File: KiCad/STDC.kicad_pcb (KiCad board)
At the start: 4 copper layers, 38 x 48 mm, 126 parts, among them IC1 TPS22916CNYFPR, IC2 TPS22916CNYFPR, IC3 R1200N001A-TR-FE, IC4 MS5849-30BA, IC5 W25Q32JWSNIQ, J1 TC2030, J2 Conn_01x03_BATT, J3 Conn_01x34_NHD_18, Q1 AO3400A, Q2 AO3400A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

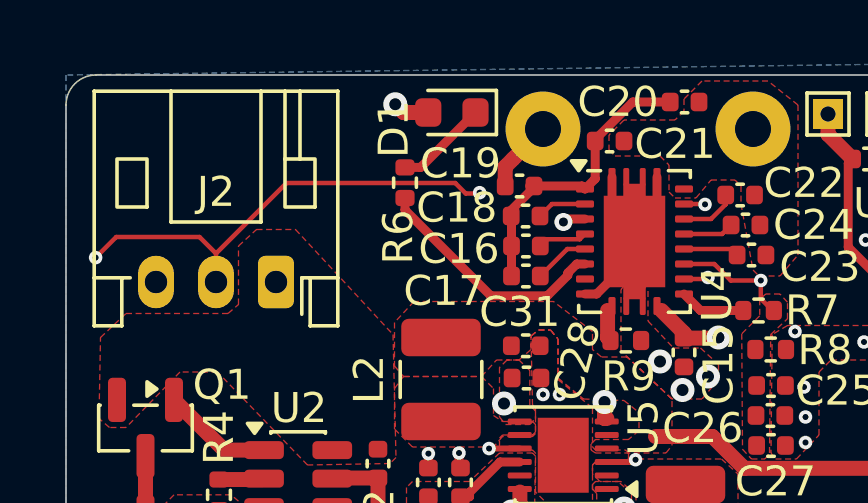
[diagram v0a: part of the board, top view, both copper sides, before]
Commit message: More space for Connector
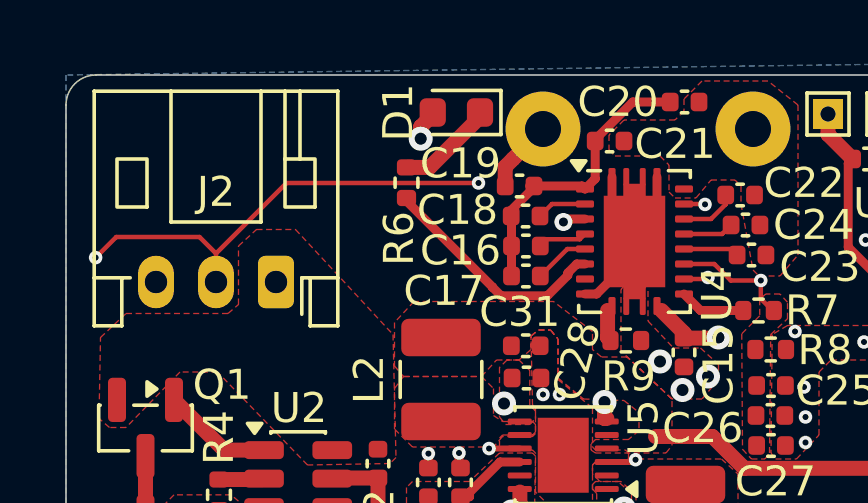
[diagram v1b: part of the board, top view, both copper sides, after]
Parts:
- moved D1 0.15 mm to (138.0, 101.8)
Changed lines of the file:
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@@
 		(tags "capacitor")
 		(property "Reference" "C16"
-			(at -2.23 0.1 0)
+			(at -2.18 0.15 0)
 			(layer "F.SilkS")
 			(effects
@@
 	(footprint "LED_SMD:LED_0603_1608Metric"
 		(layer "F.Cu")
-		(at 137.8625 101.75 180)
+		(at 138.0125 101.75 180)
 		(descr "LED SMD 0603 (1608 Metric), square (rectangular) end terminal, IPC-7351 nominal, (Body size source: http://www.tortai-tech.com/upload/download/2011102023233369053.pdf), generated with kicad-footprint-generator")
 		(tags "LED")
 		(property "Reference" "D1"
-			(at 1.9375 -0.55 90)
+			(at 1.9375 0 90)
 			(layer "F.SilkS")
 			(effects
@@
 		(tags "capacitor")
 		(property "Reference" "C18"
-			(at -2.295 -0.275 0)
+			(at -2.27 -0.2 0)
 			(layer "F.SilkS")
 			(effects
@@
 	(footprint "Resistor_SMD:R_0402_1005Metric"
 		(layer "F.Cu")
-		(at 136.3 104.09 -90)
+		(at 136.35 104.09 -90)
 		(descr "Resistor SMD 0402 (1005 Metric), square (rectangular) end terminal, IPC-7351 nominal, (Body size source: IPC-SM-782 page 72, https://www.pcb-3d.com/wordpress/wp-content/uploads/ipc-sm-782a_amendment_1_and_2.pdf), generated with kicad-footprint-generator")
 		(tags "resistor")
 		(property "Reference" "R6"
-			(at 1.81 0.225 90)
+			(at 1.86 0.25 90)
 			(layer "F.SilkS")
 			(effects
@@
 	)
 	(segment
-		(start 138.65 101.75)
-		(end 136.82 103.58)
-		(width 0.3)
+		(start 138.8 101.9)
+		(end 137.12 103.58)
+		(width 0.5)
 		(layer "F.Cu")
 		(net 20)
 	)
 	(segment
-		(start 136.82 103.58)
-		(end 136.3 103.58)
-		(width 0.3)
+		(start 136.35 103.58)
+		(end 137.12 103.58)
+		(width 0.5)
+		(layer "F.Cu")
+		(net 20)
+	)
+	(segment
+		(start 138.8 101.75)
+		(end 138.8 101.9)
+		(width 0.5)
 		(layer "F.Cu")
 		(net 20)
@@
 	)
 	(segment
-		(start 137.975 104.1)
-		(end 132.35 104.1)
+		(start 132.35 104.1)
+		(end 130 106.45)
 		(width 0.15)
 		(layer "F.Cu")
@@
 	)
 	(segment
-		(start 138.78679 104.422748)
-		(end 138.759538 104.45)
+		(start 138.75 104.1)
+		(end 132.35 104.1)
 		(width 0.15)
 		(layer "F.Cu")
@@
 	)
 	(segment
-		(start 138.759538 104.45)
-		(end 138.325 104.45)
-		(width 0.15)
-		(layer "F.Cu")
-		(net 38)
-	)
-	(segment
 		(start 146.25 107.25)
 		(end 146.2 107.3)
@@
 	)
 	(segment
-		(start 138.325 104.45)
-		(end 137.975 104.1)
-		(width 0.15)
-		(layer "F.Cu")
-		(net 38)
-	)
-	(segment
-		(start 132.35 104.1)
-		(end 130 106.45)
-		(width 0.15)
-		(layer "F.Cu")
-		(net 38)
-	)
-	(segment
 		(start 130 106.45)
 		(end 129.45 105.9)
@@
 	)
 	(via
-		(at 138.78679 104.422748)
+		(at 138.75 104.1)
 		(size 0.45)
 		(drill 0.2)
@@
 	)
 	(segment
-		(start 138.78679 104.422748)
-		(end 138.814042 104.45)
+		(start 130 106.6)
+		(end 130 107.4)
 		(width 0.15)
 		(layer "In2.Cu")
@@
 	)
 	(segment
-		(start 130 106.6)
-		(end 130 107.4)
+		(start 138.75 104.1)
+		(end 139.1 104.45)
 		(width 0.15)
 		(layer "In2.Cu")
@@
 	)
 	(segment
-		(start 138.814042 104.45)
-		(end 144.95 104.45)
+		(start 125.698176 106.876824)
+		(end 125.9875 106.5875)
 		(width 0.15)
 		(layer "In2.Cu")
@@
 	)
 	(segment
-		(start 146.8 106.85)
-		(end 146.4 107.25)
+		(start 146.8 106.3)
+		(end 146.8 106.85)
 		(width 0.15)
 		(layer "In2.Cu")
@@
 	)
 	(segment
-		(start 125.698176 106.876824)
-		(end 125.9875 106.5875)
+		(start 146.8 106.85)
+		(end 146.4 107.25)
 		(width 0.15)
 		(layer "In2.Cu")
@@
 	)
 	(segment
-		(start 128.05 121.15)
-		(end 125.698176 118.798176)
+		(start 139.1 104.45)
+		(end 144.95 104.45)
 		(width 0.15)
 		(layer "In2.Cu")
@@
 	)
 	(segment
-		(start 146.8 106.3)
-		(end 146.8 106.85)
+		(start 128.05 121.15)
+		(end 125.698176 118.798176)
 		(width 0.15)
 		(layer "In2.Cu")
@@
 	)
 	(segment
+		(start 139.219 107.569)
+		(end 136.35 104.7)
+		(width 0.3)
+		(layer "F.Cu")
+		(net 58)
+	)
+	(segment
 		(start 141.044122 107.861)
-		(end 139.161 107.861)
+		(end 139.50274 107.861)
+		(width 0.3)
+		(layer "F.Cu")
+		(net 58)
+	)
+	(segment
+		(start 139.50274 107.861)
+		(end 139.219 107.57726)
 		(width 0.3)
 		(layer "F.Cu")
@@
 	)
 	(segment
-		(start 136.3 105)
-		(end 136.3 104.6)
+		(start 139.219 107.57726)
+		(end 139.219 107.569)
 		(width 0.3)
 		(layer "F.Cu")
@@
 	)
 	(segment
-		(start 141.729 107.176122)
-		(end 141.044122 107.861)
+		(start 136.3 104.65)
+		(end 136.35 104.6)
+		(width 0.3)
+		(layer "F.Cu")
+		(net 58)
+	)
+	(segment
+		(start 136.35 104.7)
+		(end 136.35 104.6)
 		(width 0.3)
 		(layer "F.Cu")
@@
 	)
 	(segment
-		(start 142.3 106.8)
-		(end 142.024876 106.8)
+		(start 141.729 107.176122)
+		(end 141.044122 107.861)
 		(width 0.3)
 		(layer "F.Cu")
@@
 	)
 	(segment
-		(start 139.161 107.861)
-		(end 136.3 105)
+		(start 142.3 106.8)
+		(end 142.024876 106.8)
 		(width 0.3)
 		(layer "F.Cu")
@@
 	)
 	(segment
-		(start 141.7 105.3)
-		(end 142.3 105.3)
-		(width 0.3)
+		(start 136.823959 102.226041)
+		(end 137.3 101.75)
+		(width 0.5)
 		(layer "F.Cu")
 		(net 127)
 	)
 	(segment
-		(start 141.579738 105.4)
-		(end 141.6 105.4)
-		(width 0.3)
+		(start 136.823959 102.623959)
+		(end 136.823959 102.226041)
+		(width 0.5)
 		(layer "F.Cu")
 		(net 127)
 	)
 	(segment
-		(start 136.25 101.75)
-		(end 135.975 101.475)
-		(width 0.5)
+		(start 141.7 105.3)
+		(end 142.3 105.3)
+		(width 0.3)
 		(layer "F.Cu")
 		(net 127)
 	)
 	(segment
-		(start 137.075 101.75)
-		(end 136.25 101.75)
-		(width 0.5)
+		(start 141.579738 105.4)
+		(end 141.6 105.4)
+		(width 0.3)
 		(layer "F.Cu")
 		(net 127)
@@
 	)
 	(via
-		(at 135.975 101.475)
+		(at 136.823959 102.623959)
 		(size 0.8)
 		(drill 0.4)

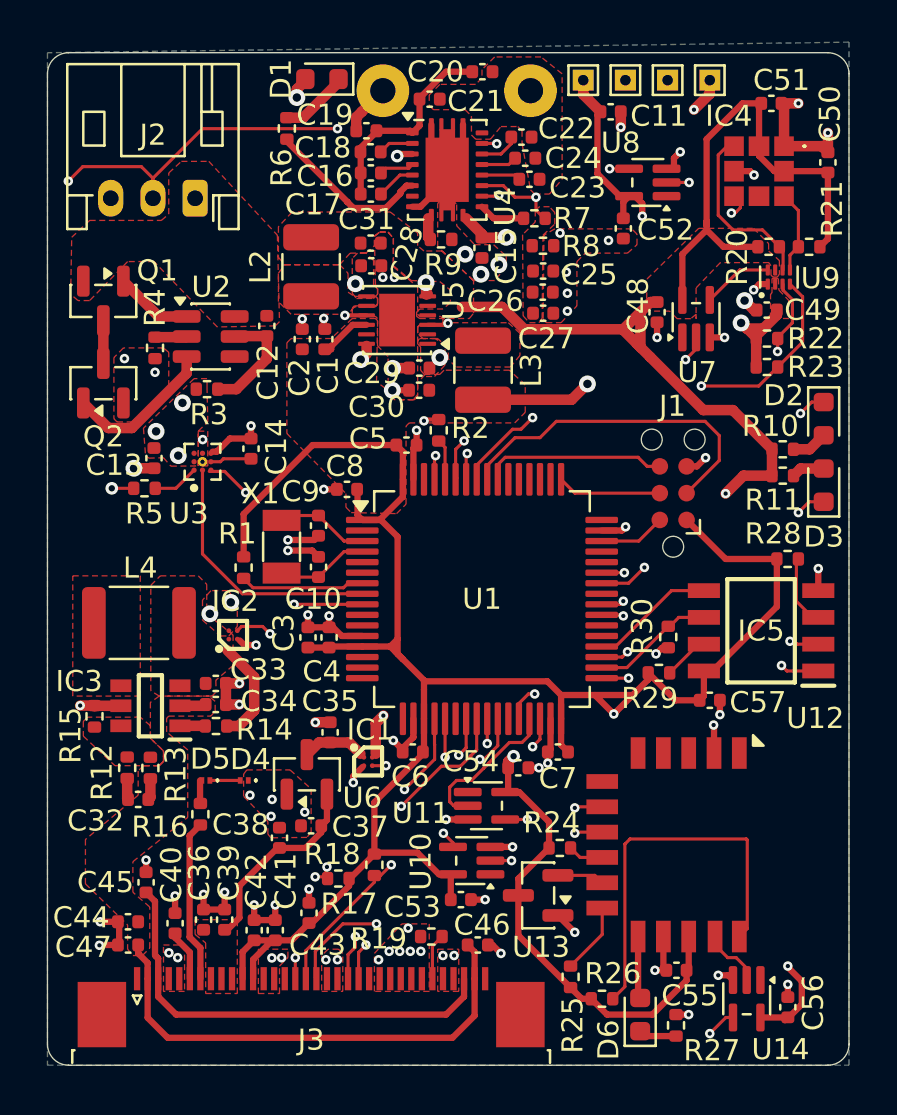
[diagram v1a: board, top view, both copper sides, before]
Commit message: Use SMD SM4 Connector for JST PH Battery
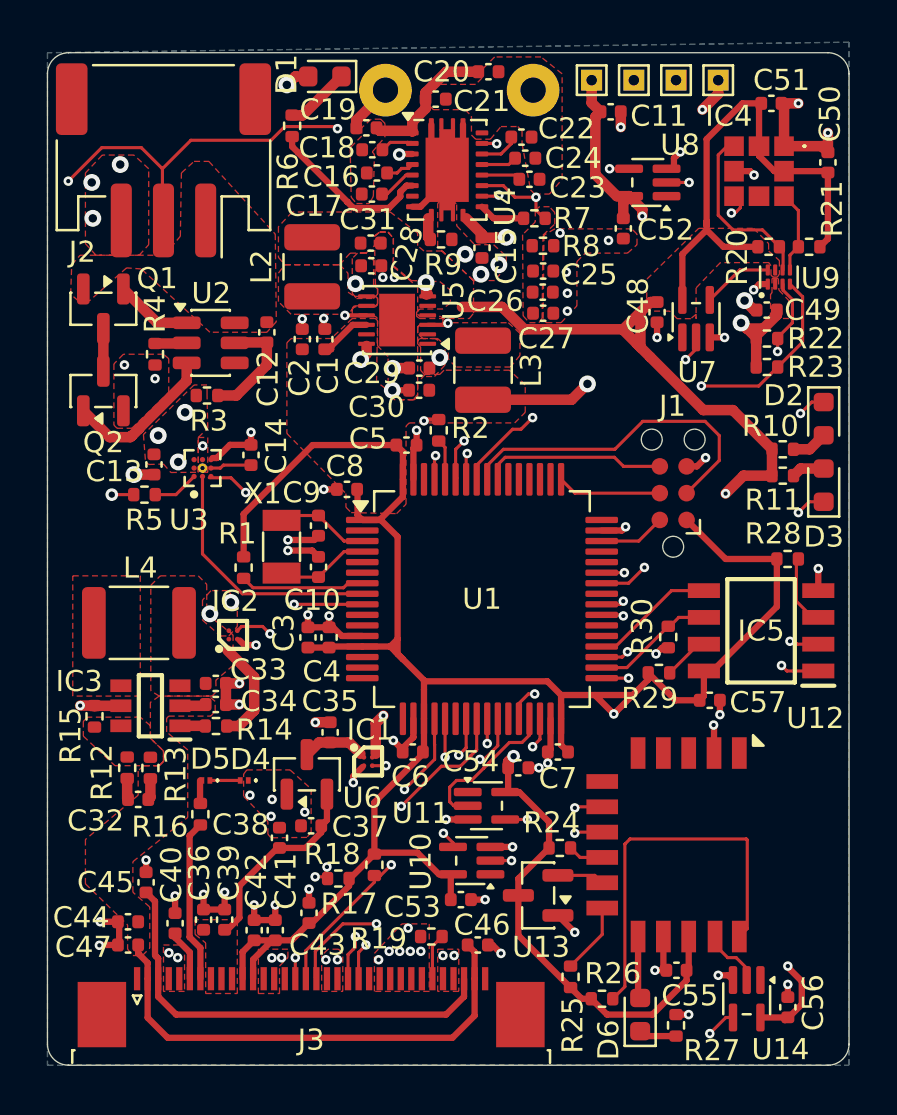
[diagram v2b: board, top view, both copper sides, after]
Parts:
- J2: footprint Connector_JST:JST_PH_S3B-PH-K_1x03_P2.00mm_Horizontal -> Connector_JST:JST_PH_S3B-PH-SM4-TB_1x03-1MP_P2.00mm_Horizontal
- moved J2 2.34 mm to (130.5, 105.6)
- moved TP1 0.40 mm to (150.8, 101.8)
- moved TP2 0.40 mm to (152.8, 101.8)
- moved TP3 0.40 mm to (154.8, 101.8)
- moved TP4 0.40 mm to (156.8, 101.8)
- moved Q1 0.37 mm to (127.7, 112.6)
- moved Q2 0.37 mm to (127.7, 116.5)
- moved C12 0.30 mm to (135.4, 113.8)
- moved C13 0.30 mm to (130.1, 120.0)
- moved C14 0.30 mm to (134.7, 119.6)
- moved R3 0.30 mm to (132.6, 116.8)
- moved R4 0.30 mm to (130.1, 114.8)
- moved R5 0.30 mm to (129.6, 121.5)
- moved U2 0.30 mm to (132.7, 114.3)
- moved U3 0.30 mm to (132.3, 120.2)
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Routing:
- net /Power+Battery/AC1: track 10.0 -> 6.92 mm
- net /Power+Battery/TS_CTRL: track 44.4 -> 44.9 mm
- net /Power+Battery/BATT+: vias 6 -> 9
- added copper zone on F.Cu, net /Power+Battery/AC1

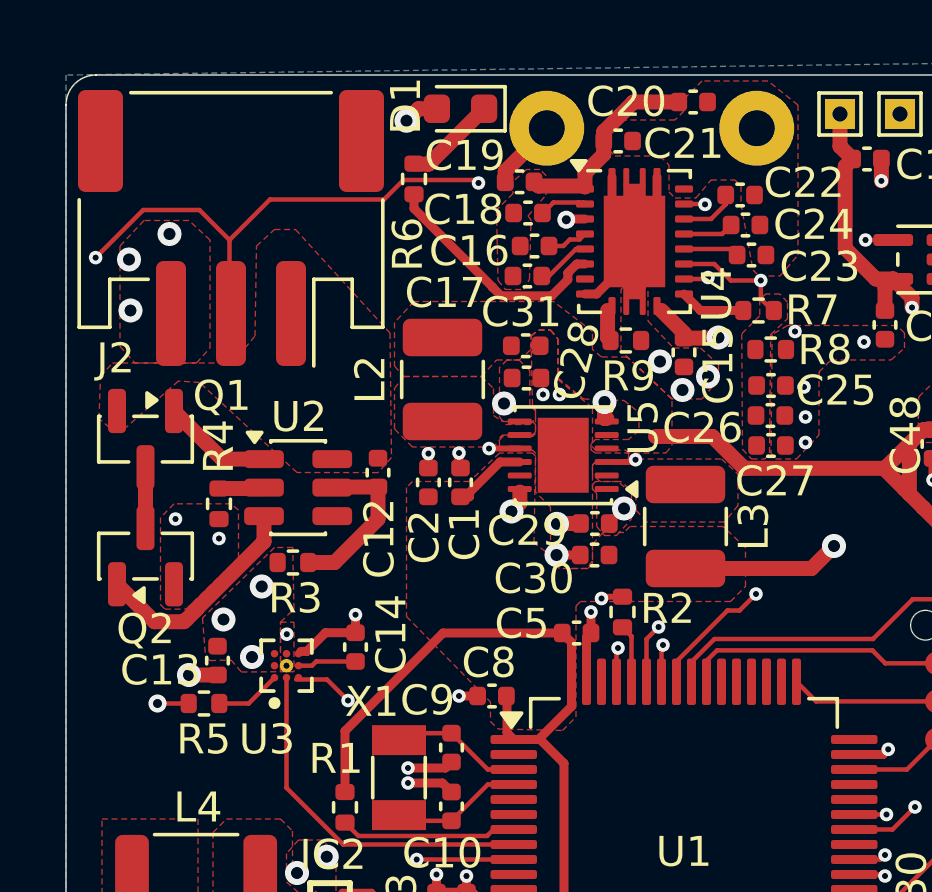
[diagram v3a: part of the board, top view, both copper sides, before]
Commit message: More space for power planes, traces
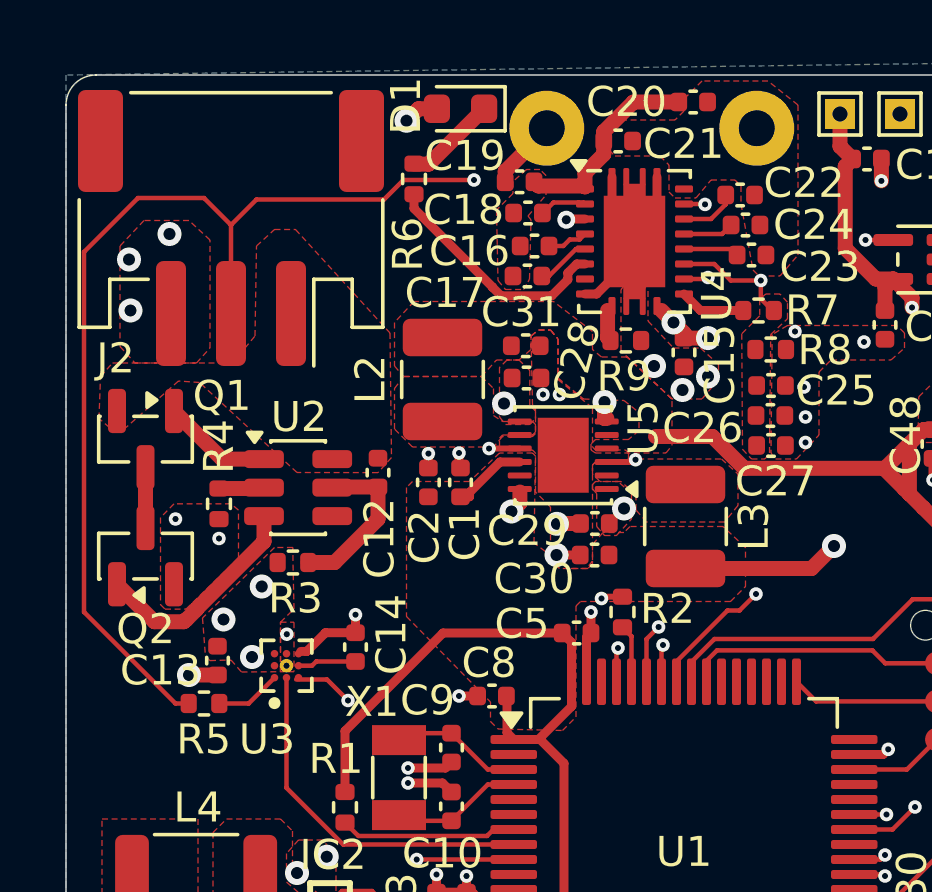
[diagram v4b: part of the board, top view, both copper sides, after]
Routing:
- net /Power+Battery/TS_CTRL: track 44.9 -> 45.8 mm, vias 4 -> 2
- net /Power+Battery/BATT+: track 4.23 -> 3.87 mm, vias 9 -> 10
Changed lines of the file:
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@@
 		(tags "capacitor")
 		(property "Reference" "C15"
-			(at 0.4 -1.15 270)
+			(at 0.4 -1.2 270)
 			(layer "F.SilkS")
 			(effects
@@
 		(tags "resistor")
 		(property "Reference" "R9"
-			(at 0.09 1.2 0)
+			(at -0.06 1.2 0)
 			(layer "F.SilkS")
 			(effects
@@
 	)
 	(via
-		(at 144.8 110.05)
+		(at 144.6 110.2)
 		(size 0.8)
 		(drill 0.4)
@@
 	)
 	(segment
-		(start 135.6 104.65)
-		(end 131.8 104.65)
+		(start 136.25 104)
+		(end 135.6 104.65)
 		(width 0.15)
 		(layer "F.Cu")
@@
 	)
 	(segment
-		(start 130.45 106)
-		(end 129.45 105)
+		(start 130.5 105.5)
+		(end 131.35 104.65)
 		(width 0.15)
 		(layer "F.Cu")
@@
 	)
 	(segment
-		(start 128.05 121.45)
-		(end 129.09 121.45)
+		(start 130.5 105.5)
+		(end 129.6 104.6)
+		(width 0.15)
+		(layer "F.Cu")
+		(net 38)
+	)
+	(segment
+		(start 130.5 108.45)
+		(end 130.5 105.5)
 		(width 0.15)
 		(layer "F.Cu")
@@
 	)
 	(segment
-		(start 138.65 104)
-		(end 138.75 104.1)
+		(start 138.6 104)
+		(end 136.25 104)
 		(width 0.15)
 		(layer "F.Cu")
@@
 	)
 	(segment
-		(start 135.6 104.65)
-		(end 136.25 104)
+		(start 129.6 104.6)
+		(end 127.4 104.6)
 		(width 0.15)
 		(layer "F.Cu")
@@
 	)
 	(segment
-		(start 136.25 104)
-		(end 138.65 104)
+		(start 127.4 104.6)
+		(end 125.6 106.4)
 		(width 0.15)
 		(layer "F.Cu")
@@
 	)
 	(segment
-		(start 146.25 107.25)
-		(end 146.2 107.3)
+		(start 135.6 104.65)
+		(end 131.35 104.65)
 		(width 0.15)
 		(layer "F.Cu")
@@
 	)
 	(segment
-		(start 129.45 105)
-		(end 127.575 105)
+		(start 146.25 107.25)
+		(end 146.2 107.3)
 		(width 0.15)
 		(layer "F.Cu")
@@
 	)
 	(segment
-		(start 130.45 108.35)
-		(end 130.45 106)
+		(start 138.65 104)
+		(end 138.6 104)
 		(width 0.15)
 		(layer "F.Cu")
@@
 	)
 	(segment
-		(start 131.8 104.65)
-		(end 130.45 106)
+		(start 125.6 118.4)
+		(end 128.65 121.45)
 		(width 0.15)
 		(layer "F.Cu")
@@
 	)
 	(segment
-		(start 127.575 105)
-		(end 125.9875 106.5875)
+		(start 128.65 121.45)
+		(end 129.09 121.45)
 		(width 0.15)
 		(layer "F.Cu")
 		(net 38)
 	)
-	(via
-		(at 125.9875 106.5875)
-		(size 0.45)
-		(drill 0.2)
-		(layers "F.Cu" "B.Cu")
+	(segment
+		(start 125.6 106.4)
+		(end 125.6 118.4)
+		(width 0.15)
+		(layer "F.Cu")
 		(net 38)
 	)
 	(via
-		(at 138.75 104.1)
+		(at 138.6 104)
 		(size 0.45)
 		(drill 0.2)
@@
 	)
 	(via
-		(at 128.05 121.45)
-		(size 0.6)
-		(drill 0.3)
-		(layers "F.Cu" "B.Cu")
-		(net 38)
-	)
-	(via
 		(at 146.4 107.25)
 		(size 0.45)
@@
 	)
 	(segment
-		(start 125.9875 106.5875)
-		(end 125.698176 106.876824)
-		(width 0.15)
-		(layer "In2.Cu")
-		(net 38)
-	)
-	(segment
-		(start 144.95 104.45)
-		(end 146.8 106.3)
-		(width 0.15)
-		(layer "In2.Cu")
-		(net 38)
-	)
-	(segment
-		(start 138.75 104.1)
-		(end 139.1 104.45)
-		(width 0.15)
-		(layer "In2.Cu")
-		(net 38)
-	)
-	(segment
-		(start 125.698176 106.876824)
-		(end 125.698176 119.098176)
-		(width 0.15)
-		(layer "In2.Cu")
-		(net 38)
-	)
-	(segment
-		(start 146.8 106.3)
-		(end 146.8 106.85)
+		(start 144.8 104)
+		(end 146.8 106)
 		(width 0.15)
 		(layer "In2.Cu")
@@
 	)
 	(segment
-		(start 139.1 104.45)
-		(end 144.95 104.45)
+		(start 138.6 104)
+		(end 144.8 104)
 		(width 0.15)
 		(layer "In2.Cu")
@@
 	)
 	(segment
-		(start 125.698176 119.098176)
-		(end 128.05 121.45)
+		(start 146.8 106)
+		(end 146.8 106.85)
 		(width 0.15)
 		(layer "In2.Cu")
@@
 	)
 	(segment
-		(start 145.6 109.1)
-		(end 144.847441 108.347441)
-		(width 0.5)
+		(start 141.7 105.3)
+		(end 142.3 105.3)
+		(width 0.3)
 		(layer "F.Cu")
 		(net 127)
 	)
 	(segment
-		(start 146.73 109.27)
-		(end 146.75 109.25)
+		(start 146.4 109.27)
+		(end 145.6 109.27)
 		(width 0.5)
 		(layer "F.Cu")
@@
 	)
 	(segment
-		(start 145.6 109.27)
-		(end 146.73 109.27)
+		(start 145.25 108.75)
+		(end 144.847441 108.347441)
 		(width 0.5)
 		(layer "F.Cu")
@@
 	)
 	(segment
-		(start 141.7 105.3)
-		(end 142.3 105.3)
-		(width 0.3)
+		(start 145.6 109.1)
+		(end 145.6 109.27)
+		(width 0.5)
 		(layer "F.Cu")
 		(net 127)
@@
 	)
 	(segment
-		(start 145.6 109.27)
+		(start 145.25 108.75)
 		(end 145.6 109.1)
 		(width 0.5)
@@
 	)
 	(via
-		(at 146.75 109.25)
+		(at 146.4 109.27)
 		(size 0.8)
 		(drill 0.4)
@@
 	)
 	(via
+		(at 145.25 108.75)
+		(size 0.8)
+		(drill 0.4)
+		(layers "F.Cu" "B.Cu")
+		(net 127)
+	)
+	(via
 		(at 136.35 102.025)
 		(size 0.8)
@@
 		(polygon
 			(pts
-				(xy 138.5 104.65) (xy 137.875 104) (xy 137.8 102) (xy 137.175 101.15) (xy 129.2 101.15) (xy 126.4 103.7)
-				(xy 126.35 118.05) (xy 128.9 120.4) (xy 132.1 120.4) (xy 132.1 117.6) (xy 139.65 109.8) (xy 146.8 109.85)
-				(xy 147.25 109.4) (xy 147.25 108.85) (xy 145.95 107.6) (xy 145.95 105.825) (xy 144.6 104.6)
+				(xy 138.8 104.4) (xy 138.2 104) (xy 138.2 102) (xy 137.4 101.15) (xy 129.2 101.15) (xy 125.6 104.6)
+				(xy 125.625 117.2) (xy 128.9 120.4) (xy 132.1 120.4) (xy 132.1 117.6) (xy 139.65 109.8) (xy 147.4 109.85)
+				(xy 147.6 109.6) (xy 147.6 108.8) (xy 145.95 107.2) (xy 145.95 105.4) (xy 145 104.4)
 			)
 		)
